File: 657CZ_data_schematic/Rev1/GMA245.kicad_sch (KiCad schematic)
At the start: 2 parts

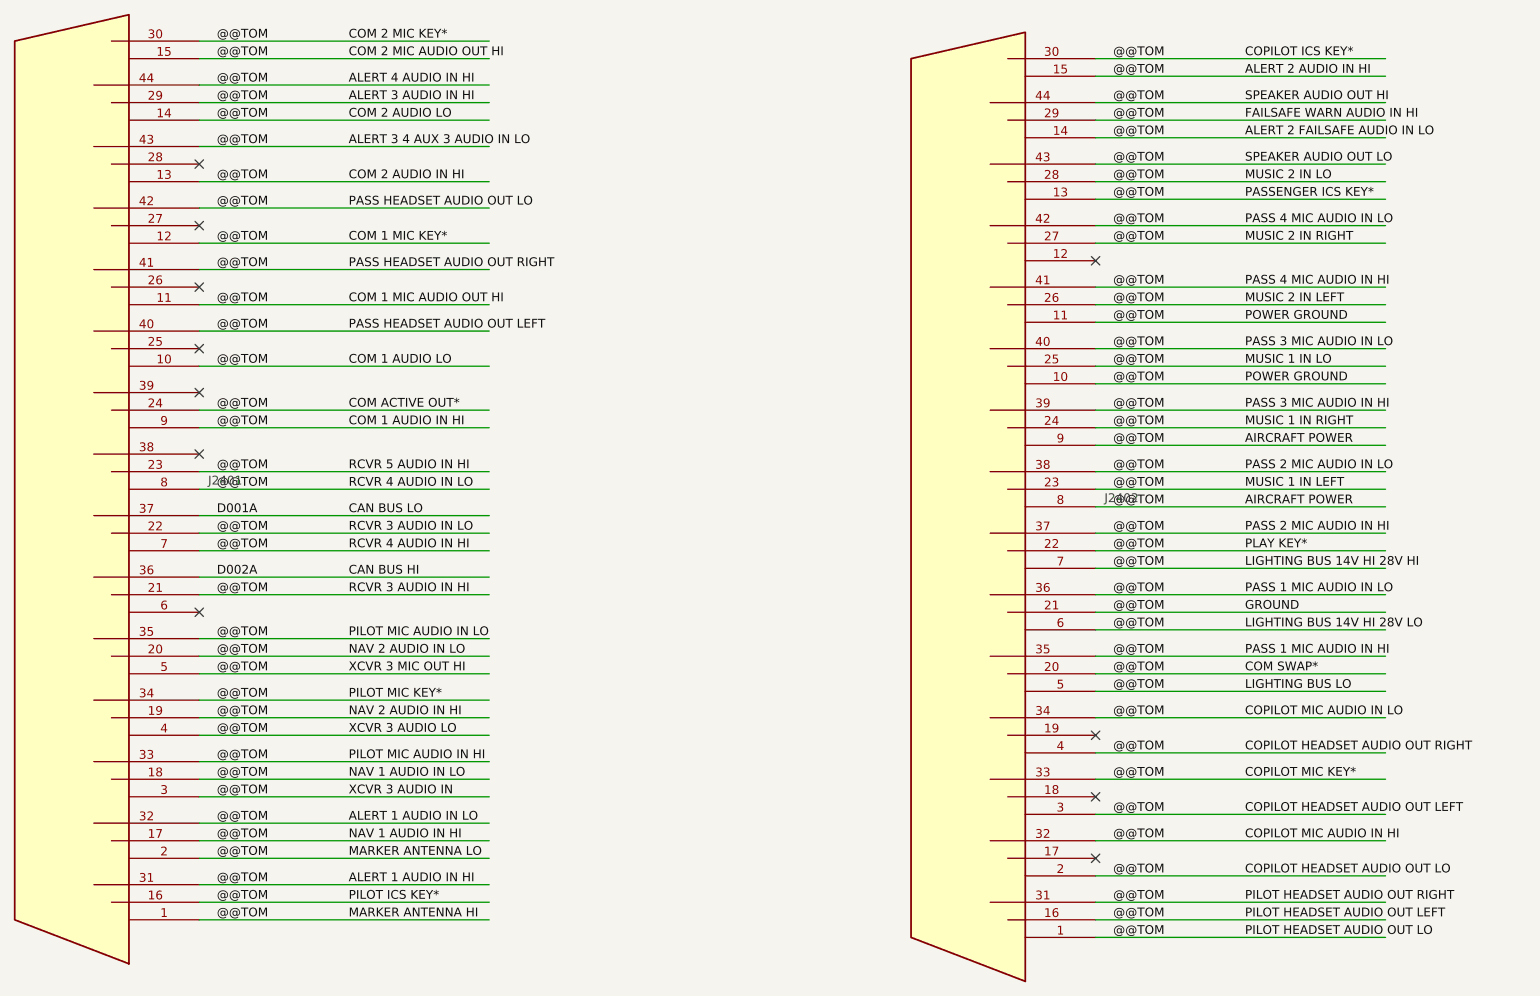
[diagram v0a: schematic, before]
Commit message: added data connections after AvClassics wiring. completed LRUs GMU, GDU, GSU, GAD, GNC, GTX, GTR  Not completed GMA, GEA and autopilot LRUs
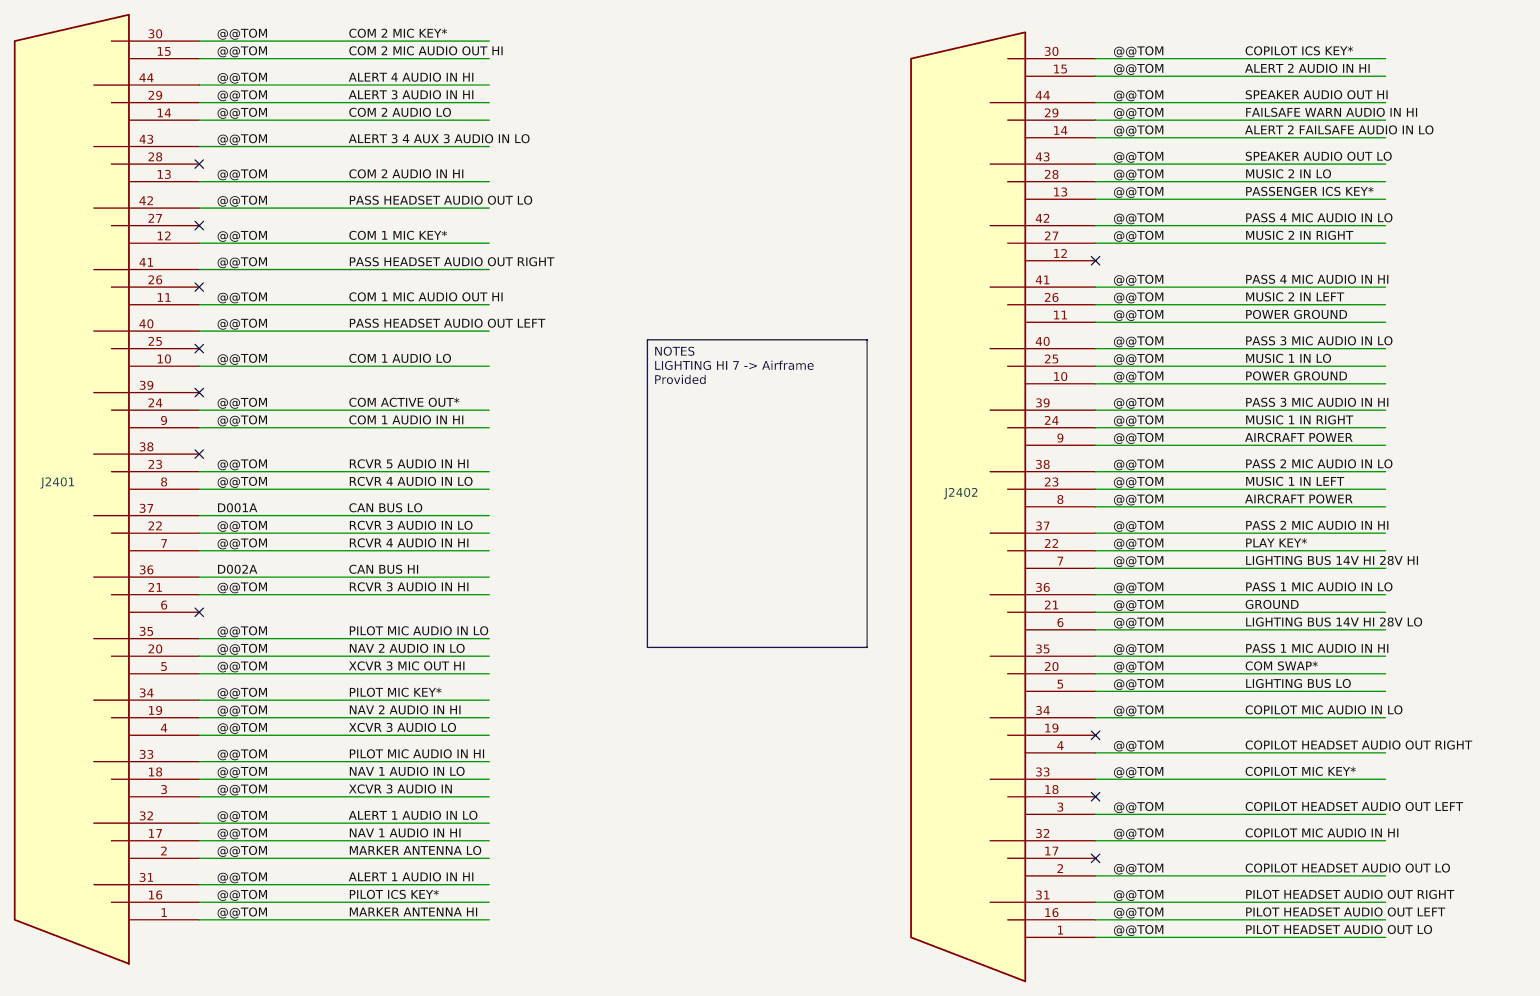
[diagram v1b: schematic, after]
